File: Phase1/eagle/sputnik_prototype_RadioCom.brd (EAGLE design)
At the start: 99 x 100 mm, 104 parts, among them Y1 32MHz

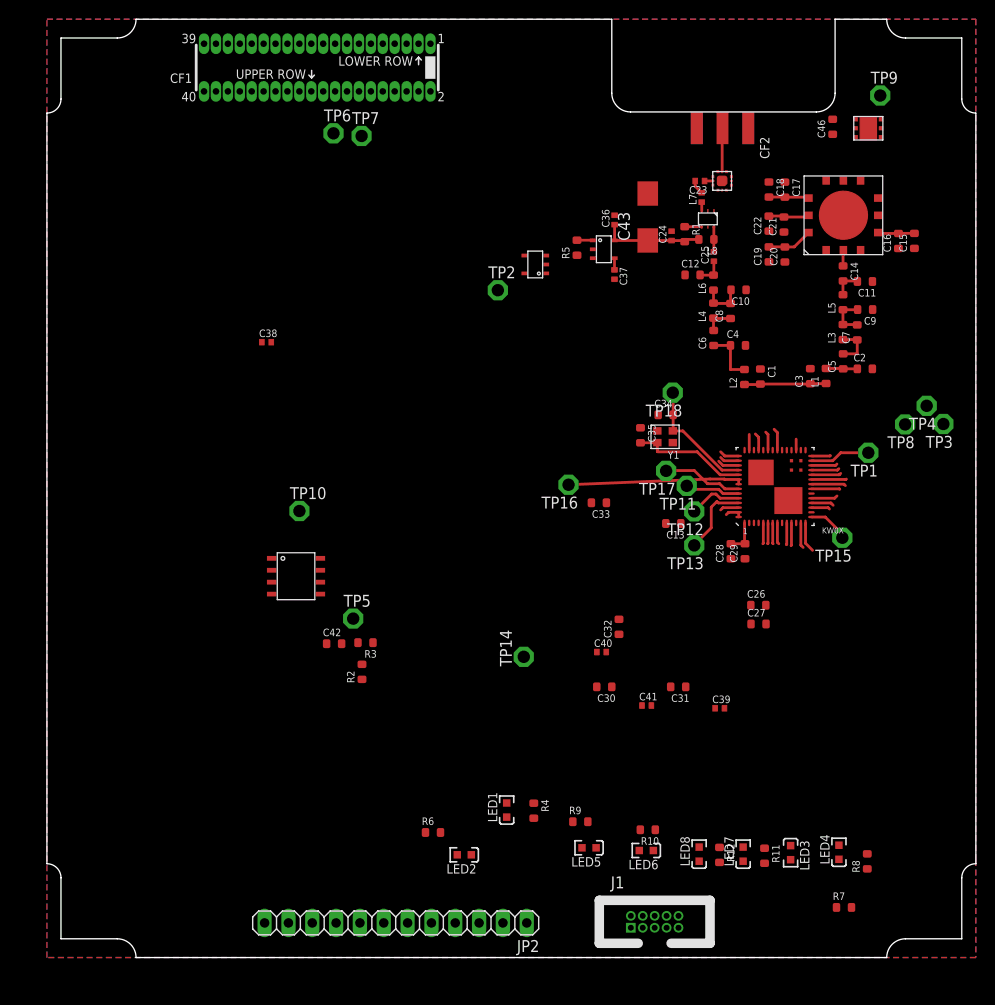
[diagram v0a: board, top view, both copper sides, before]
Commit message: Organized LED locations, test points, need to talk to Glenn about crossing RF paths because the switch inputs are reverse of the RFIO and PA_BOOST outputs.
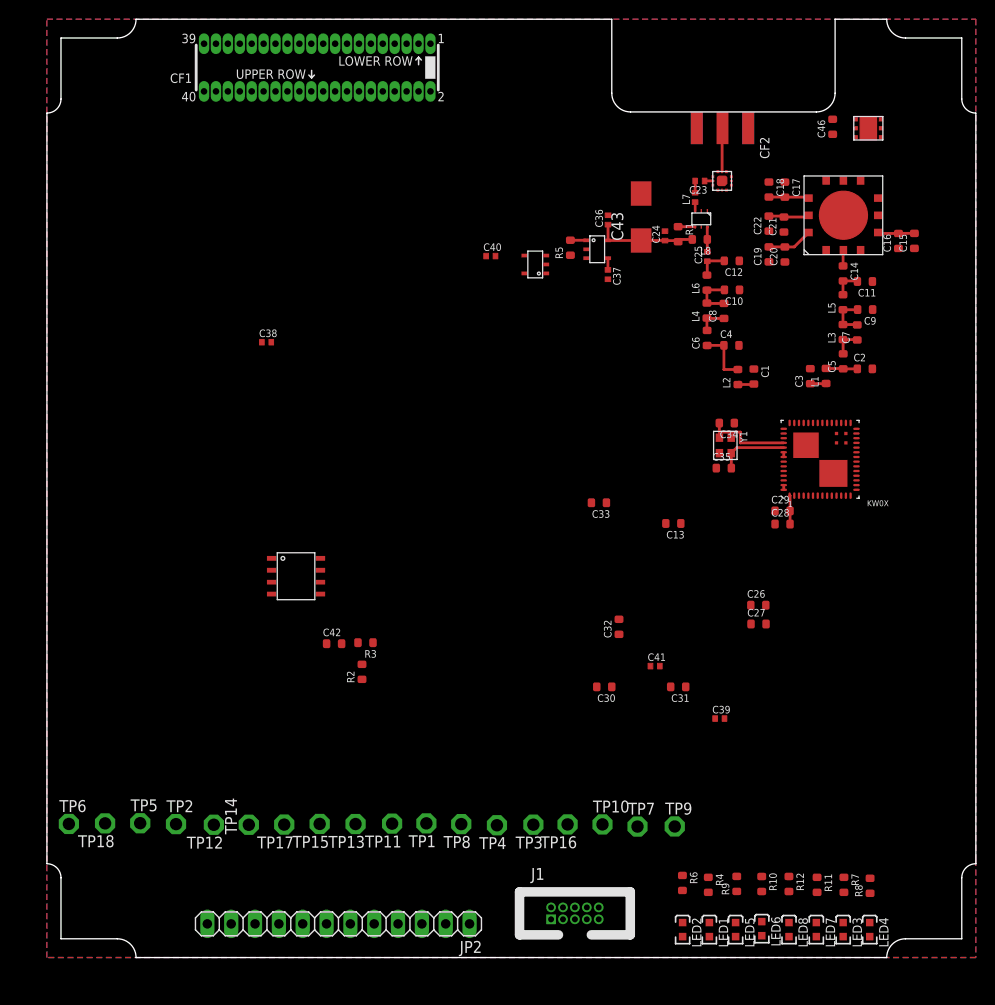
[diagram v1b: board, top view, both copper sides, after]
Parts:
- moved TP9 80.9 mm to (66.9, 14.0)
- moved TP7 79.3 mm to (62.9, 14.0)
- moved TP6 78.8 mm to (2.34, 14.2)
- moved TP18 75.9 mm to (6.20, 14.3)
- moved TP2 66.4 mm to (13.8, 14.2)
- moved TP4 64.0 mm to (48.0, 14.1)
- moved TP8 63.7 mm to (44.2, 14.2)
- moved TP15 63.5 mm to (29.1, 14.2)
- moved TP1 61.5 mm to (40.4, 14.3)
- moved TP12 61.1 mm to (17.8, 14.2)
- moved TP3 61.1 mm to (51.8, 14.2)
- moved TP17 55.5 mm to (25.3, 14.2)
- moved TP11 47.8 mm to (36.8, 14.3)
- moved TP13 46.7 mm to (32.9, 14.2)
- moved TP10 46.5 mm to (59.2, 14.2)
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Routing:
- net DIO0: track 18.7 -> 0.50 mm
- net 3.3V: track 13.0 -> 3.57 mm
- net DIO1: track 8.55 -> 0.00 mm
- net N$9: track 8.05 -> 0.00 mm
- net DIO5/CLKOUT: track 6.46 -> 0.00 mm
- net !CS: track 6.41 -> 0.00 mm
- net N$3: track 6.09 -> 0.00 mm
- net N$5: track 5.68 -> 0.00 mm
- net VR_PA: track 9.33 -> 4.01 mm
- net N$8: track 12.4 -> 7.45 mm
- net PTC4: track 3.74 -> 0.00 mm
- net PTB17: track 3.68 -> 0.00 mm
- net UART0_RX: track 3.23 -> 0.00 mm
- net PTC1: track 3.18 -> 0.00 mm
- net PTB2: track 3.04 -> 0.00 mm
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
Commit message: Attached SPI cache
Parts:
- moved C42 65.0 mm to (90.7, 58.4), turned to 270 degrees
- moved R2 64.7 mm to (91.9, 58.4)
- moved U$1 62.6 mm to (90.1, 54.9), turned to 0 degrees
- moved R3 60.8 mm to (93.2, 47.3), turned to 270 degrees
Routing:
- net MOSI: track 0.00 -> 19.4 mm
- net MISO: track 0.00 -> 18.5 mm, vias 0 -> 2
- net SCLK: track 0.00 -> 15.5 mm
- net !CS: track 0.00 -> 10.1 mm
- net !HOLD: track 0.00 -> 2.17 mm
- net N$11: track 0.00 -> 2.16 mm
- net 3.3V: track 3.57 -> 5.72 mm
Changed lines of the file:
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@@
 <attribute name="MFN-PN" value="AAT3215" x="57.86" y="74.06" size="1.778" layer="27" rot="R90" display="off"/>
 </element>
-<element name="U$1" library="psas_c3_team05" package="W25Q80DV" value="W25Q80DV" x="28.55" y="43.14" rot="R270"/>
-<element name="C42" library="rcl_custom" package=".0603-B-NOSILK" value="100nF" x="30.61" y="33.45"/>
+<element name="U$1" library="psas_c3_team05" package="W25Q80DV" value="W25Q80DV" x="90.06" y="54.85"/>
+<element name="C42" library="rcl_custom" package=".0603-B-NOSILK" value="100nF" x="90.65" y="58.39" rot="R270"/>
 <element name="TP9" library="testpad" package="P1-13" value="TPSPAD1-13" x="66.91" y="13.97">
 <attribute name="TP_SIGNAL_NAME" value="" x="66.91" y="13.97" size="1.778" layer="27" display="off"/>
@@
 <attribute name="TP_SIGNAL_NAME" value="" x="25.29" y="14.17" size="1.778" layer="27" rot="R180" display="off"/>
 </element>
-<element name="R2" library="rcl_custom" package=".0603-B-NOSILK" value="10k" x="33.58" y="30.45" rot="R90"/>
-<element name="R3" library="rcl_custom" package=".0603-B-NOSILK" value="10k" x="33.95" y="33.56" rot="R180"/>
+<element name="R2" library="rcl_custom" package=".0603-B-NOSILK" value="10k" x="91.9" y="58.4" rot="R90"/>
+<element name="R3" library="rcl_custom" package=".0603-B-NOSILK" value="10k" x="93.2" y="47.3" rot="R270"/>
 <element name="LED1" library="psas_c3_team05" package="LED-0603" value="" x="70.6" y="2.98" rot="R270">
 <attribute name="GREEN" value="" x="70.6" y="2.98" size="1.778" layer="27" rot="R270" display="off"/>
@@
 <wire x1="67.73" y1="8.75" x2="70.49" y2="8.55" width="0" layer="19" extent="1-1"/>
 <wire x1="17.1" y1="3.59" x2="67.73" y2="8.75" width="0" layer="19" extent="1-1"/>
-<wire x1="29.81" y1="33.45" x2="67.73" y2="8.75" width="0" layer="19" extent="1-1"/>
-<wire x1="23.95" y1="38.735" x2="29.81" y2="33.45" width="0" layer="19" extent="1-1"/>
-<wire x1="23.91" y1="65.58" x2="23.95" y2="38.735" width="0" layer="19" extent="1-1"/>
+<wire x1="90.65" y1="59.19" x2="67.73" y2="8.75" width="0" layer="19" extent="1-1"/>
+<wire x1="94.465" y1="50.25" x2="90.65" y2="59.19" width="0" layer="19" extent="1-1"/>
+<wire x1="23.91" y1="65.58" x2="94.465" y2="50.25" width="0" layer="19" extent="1-1"/>
 <wire x1="18.015" y1="92.31" x2="23.91" y2="65.58" width="0" layer="19" extent="1-1"/>
 <wire x1="16.745" y1="92.31" x2="18.015" y2="92.31" width="0" layer="19" extent="1-1"/>
@@
 <wire x1="53.73" y1="4.075" x2="87.69" y2="2.23" width="0" layer="19" extent="1-1"/>
 <wire x1="42.5" y1="3.59" x2="53.73" y2="4.075" width="0" layer="19" extent="1-1"/>
-<wire x1="33.58" y1="31.25" x2="58.6" y2="28.85" width="0" layer="19" extent="1-1"/>
-<wire x1="33.15" y1="33.56" x2="33.58" y2="31.25" width="0" layer="19" extent="1-1"/>
-<wire x1="31.41" y1="33.45" x2="33.15" y2="33.56" width="0" layer="19" extent="1-1"/>
-<wire x1="29.15" y1="42.545" x2="31.41" y2="33.45" width="0" layer="19" extent="1-1"/>
+<wire x1="91.9" y1="59.2" x2="58.6" y2="28.85" width="0" layer="19" extent="1-1"/>
+<wire x1="93.2" y1="46.5" x2="91.9" y2="59.2" width="0" layer="19" extent="1-1"/>
+<wire x1="90.65" y1="57.59" x2="93.2" y2="46.5" width="0" layer="19" extent="1-1"/>
 <wire x1="50.88" y1="72.915" x2="78.5222" y2="56.35" width="0" layer="19" extent="1-1"/>
 <wire x1="79.15" y1="49.2222" x2="79.2" y2="49.2222" width="0.3" layer="1"/>
 <wire x1="79.2" y1="49.2222" x2="79.2" y2="47.6" width="0.3" layer="1"/>
 <wire x1="79.2" y1="47.6" x2="79.2" y2="46.2" width="0.3" layer="1"/>
+<wire x1="90.655" y1="55.45" x2="90.65" y2="55.45" width="0.3" layer="1"/>
+<wire x1="90.65" y1="55.45" x2="90.65" y2="57.59" width="0.3" layer="1"/>
 </signal>
 <signal name="N$7">
@@
 <contactref element="TP10" pad="TP"/>
 <contactref element="R2" pad="1"/>
-<wire x1="33.58" y1="29.65" x2="29.15" y2="41.275" width="0" layer="19" extent="1-1"/>
-<wire x1="59.21" y1="14.19" x2="29.15" y2="41.275" width="0" layer="19" extent="1-1"/>
+<wire x1="59.21" y1="14.19" x2="91.925" y2="55.45" width="0" layer="19" extent="1-1"/>
+<wire x1="91.925" y1="55.45" x2="91.9" y2="55.45" width="0.3" layer="1"/>
+<wire x1="91.9" y1="55.45" x2="91.9" y2="57.6" width="0.3" layer="1"/>
 </signal>
 <signal name="!CS">
@@
 <contactref element="KW0X" pad="27"/>
 <contactref element="TP1" pad="TP"/>
-<wire x1="23.95" y1="42.545" x2="86.2778" y2="55.85" width="0" layer="19" extent="1-1"/>
-<wire x1="40.44" y1="14.3" x2="23.95" y2="42.545" width="0" layer="19" extent="1-1"/>
+<wire x1="40.44" y1="14.3" x2="90.655" y2="50.25" width="0" layer="19" extent="1-1"/>
+<wire x1="86.2778" y1="55.85" x2="89.7" y2="55.85" width="0.3" layer="1"/>
+<wire x1="89.7" y1="55.85" x2="89.7" y2="50.2" width="0.3" layer="1"/>
+<wire x1="89.7" y1="50.2" x2="90.655" y2="50.2" width="0.3" layer="1"/>
+<wire x1="90.655" y1="50.2" x2="90.655" y2="50.25" width="0.3" layer="1"/>
 </signal>
 <signal name="SCLK">
@@
 <contactref element="KW0X" pad="28"/>
 <contactref element="TP2" pad="TP"/>
-<wire x1="29.15" y1="40.005" x2="86.2778" y2="56.35" width="0" layer="19" extent="1-1"/>
-<wire x1="13.76" y1="14.22" x2="29.15" y2="40.005" width="0" layer="19" extent="1-1"/>
+<wire x1="13.76" y1="14.22" x2="93.195" y2="55.45" width="0" layer="19" extent="1-1"/>
+<wire x1="86.2778" y1="56.35" x2="89.7" y2="56.35" width="0.3" layer="1"/>
+<wire x1="89.7" y1="56.35" x2="89.7" y2="60.2" width="0.3" layer="1"/>
+<wire x1="89.7" y1="60.2" x2="93.195" y2="60.2" width="0.3" layer="1"/>
+<wire x1="93.195" y1="60.2" x2="93.195" y2="55.45" width="0.3" layer="1"/>
 </signal>
 <signal name="MISO">
@@
 <contactref element="KW0X" pad="29"/>
 <contactref element="TP3" pad="TP"/>
-<wire x1="23.95" y1="41.275" x2="85.65" y2="56.9778" width="0" layer="19" extent="1-1"/>
-<wire x1="51.84" y1="14.16" x2="23.95" y2="41.275" width="0" layer="19" extent="1-1"/>
+<wire x1="51.84" y1="14.16" x2="91.925" y2="50.25" width="0" layer="19" extent="1-1"/>
+<wire x1="85.65" y1="56.9778" x2="85.65" y2="57.8" width="0.3" layer="1"/>
+<wire x1="85.65" y1="57.8" x2="87.7" y2="57.8" width="0.3" layer="1"/>
+<via x="87.7" y="57.8" extent="1-16" drill="0.6" shape="octagon"/>
+<wire x1="87.7" y1="57.8" x2="87.7" y2="48.3" width="0.3" layer="16"/>
+<wire x1="87.7" y1="48.3" x2="91.9" y2="48.3" width="0.3" layer="16"/>
+<via x="91.9" y="48.3" extent="1-16" drill="0.6" shape="octagon"/>
+<wire x1="91.9" y1="48.3" x2="91.9" y2="50.25" width="0.3" layer="1"/>
+<wire x1="91.9" y1="50.25" x2="91.925" y2="50.25" width="0.3" layer="1"/>
 </signal>
 <signal name="MOSI">
@@
 <contactref element="KW0X" pad="31"/>
 <contactref element="TP4" pad="TP"/>
-<wire x1="29.15" y1="38.735" x2="84.65" y2="56.9778" width="0" layer="19" extent="1-1"/>
-<wire x1="47.96" y1="14.1" x2="29.15" y2="38.735" width="0" layer="19" extent="1-1"/>
+<wire x1="47.96" y1="14.1" x2="94.465" y2="55.45" width="0" layer="19" extent="1-1"/>
+<wire x1="84.65" y1="56.9778" x2="84.65" y2="58.6" width="0.3" layer="1"/>
+<wire x1="84.65" y1="58.6" x2="88.8" y2="58.6" width="0.3" layer="1"/>
+<wire x1="88.8" y1="58.6" x2="88.8" y2="61" width="0.3" layer="1"/>
+<wire x1="88.8" y1="61" x2="94.4" y2="61" width="0.3" layer="1"/>
+<wire x1="94.4" y1="61" x2="94.4" y2="55.45" width="0.3" layer="1"/>
+<wire x1="94.4" y1="55.45" x2="94.465" y2="55.45" width="0.3" layer="1"/>
 </signal>
 <signal name="PTC7">
@@
 <contactref element="R3" pad="1"/>
 <contactref element="TP5" pad="TP"/>
-<wire x1="23.95" y1="40.005" x2="34.75" y2="33.56" width="0" layer="19" extent="1-1"/>
-<wire x1="9.94" y1="14.32" x2="23.95" y2="40.005" width="0" layer="19" extent="1-1"/>
+<wire x1="9.94" y1="14.32" x2="93.195" y2="50.25" width="0" layer="19" extent="1-1"/>
+<wire x1="93.195" y1="50.25" x2="93.2" y2="50.25" width="0.3" layer="1"/>
+<wire x1="93.2" y1="50.25" x2="93.2" y2="48.1" width="0.3" layer="1"/>
 </signal>
 <signal name="N$12">

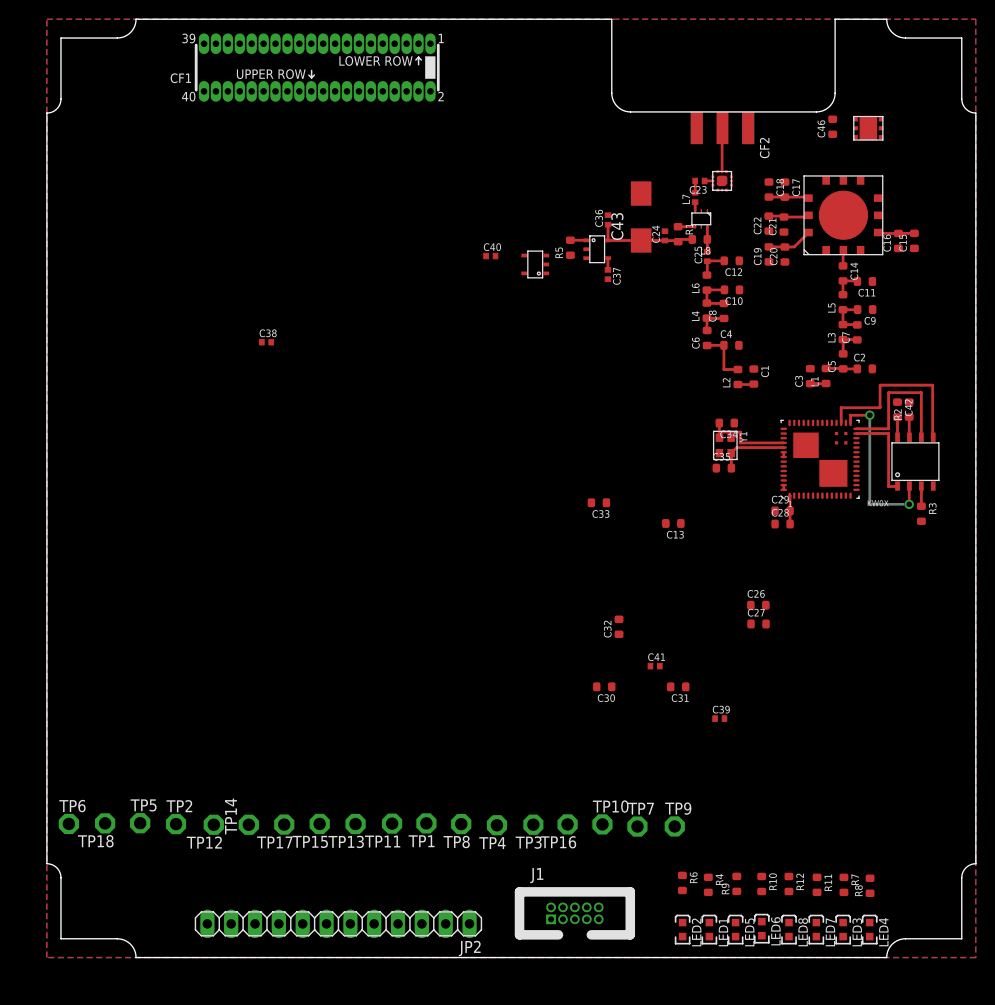
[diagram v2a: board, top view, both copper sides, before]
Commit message: Poor Jake. It's like there's some crazy guy screwing with him every time he commits... oh, wait. Huh. Anyway. Updated board outline with keepouts. Moved connectors into position and locked. Added shield over LNA (how could this be a bad idea? maybe the PA could use a sheild too, but with heat sinking?). Uncrossed the streams: make sure your main RF lines never, ever dive through the board. That sucks, keep it to one layer. So I had to move the PA and LNA around. Still needs some cleanup, but it's OK. Put resistors for sensitive supplies by the supplies, so no stray low impedance leakage.
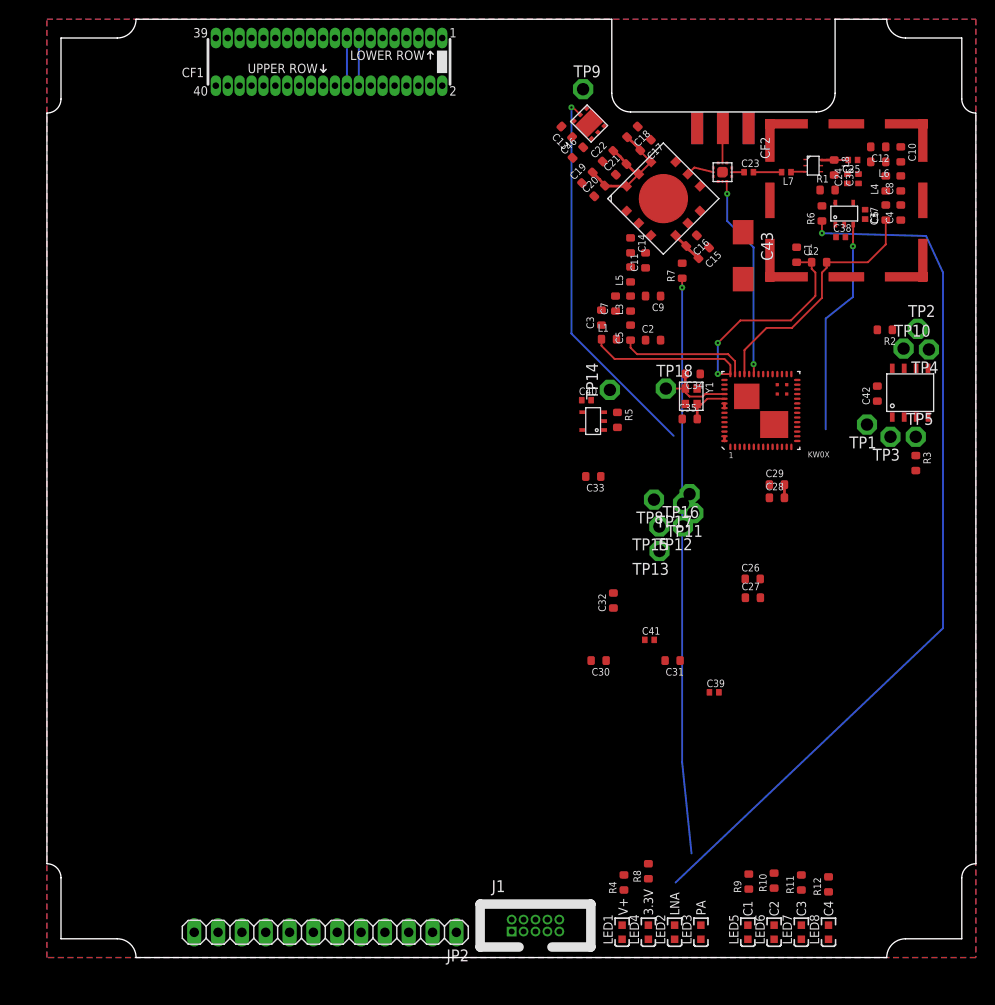
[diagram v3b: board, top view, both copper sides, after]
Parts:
- removed TP6, TP7: TPSPAD1-13, testpad:P1-13
- added SH1: BMI-S-202-SHIELD, hw-laird-bmi-s-202:BMI-S-202
- moved TP2 95.0 mm to (92.8, 67.0)
- moved TP5 92.3 mm to (92.6, 55.5)
- moved TP9 79.2 mm to (57.1, 92.5)
- moved TP18 75.6 mm to (66.0, 60.6), turned to 0 degrees
- moved R6 72.9 mm to (82.6, 79.3), turned to 90 degrees
- moved TP4 68.5 mm to (94.0, 64.8)
- moved R7 67.7 mm to (67.7, 73.2), turned to 90 degrees
- moved TP1 63.3 mm to (87.4, 56.8)
- moved C38 62.2 mm to (84.6, 76.8)
- moved TP14 60.2 mm to (60.0, 60.5)
- moved TP10 60.0 mm to (91.3, 64.9)
- moved TP12 59.3 mm to (67.8, 46.0)
- moved TP3 56.2 mm to (89.9, 55.5)
- moved TP17 54.6 mm to (67.8, 48.4)
- moved TP15 48.1 mm to (65.3, 45.9)
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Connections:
- removed net N$26: LED5.K, R9.2
- removed net N$29: LED6.K, R10.2
- removed net N$33: LED8.K, R12.2
- new net N$23: LED8.A, R12.1
- new net V_LNA_FILTERED: LED2.A, R6.1
- new net V_PA_FILTERED: LED3.A, R7.1
- net 3.3V: now also R8.2; no longer LED4.A
- net GND: now also LED1.K, LED2.K, LED3.K, LED4.K, LED5.K, LED6.K, LED7.K, LED8.K, SH1.P$1, SH1.P$10, SH1.P$11, SH1.P$12, SH1.P$2, SH1.P$3, SH1.P$4, SH1.P$5, SH1.P$6, SH1.P$7, SH1.P$8, SH1.P$9; no longer R10.1, R11.1, R12.1, R4.1, R6.1, R7.1, R8.1, R9.1
- net LNA_IN: now also TRSWITCH.2; no longer TRSWITCH.8
- net N$14: now also LED1.A, R4.1; no longer LED1.K, R4.2
- net N$15: now also LED5.A, R9.1; no longer LED2.K, R6.2
- net N$2: now also TRSWITCH.8; no longer TRSWITCH.2
- net N$20: now also LED6.A, R10.1; no longer LED3.K, R7.2
- net N$21: now also LED7.A, R11.1; no longer LED7.K, R11.2
- net N$22: now also LED4.A, R8.1; no longer LED4.K, R8.2
- net PTC1: now also R9.2; no longer LED5.A
- net PTC2: now also R10.2; no longer LED6.A
- net PTC3: now also R11.2; no longer LED7.A
- net PTC4: now also R12.2; no longer LED8.A
- net UART0_RX: no longer TP6.TP
- net UART0_TX: no longer TP7.TP
- net V+: now also R4.2; no longer LED1.A
- net VBIAS: now also R6.2; no longer LED2.A
- net VPA: now also R7.2; no longer LED3.A
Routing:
- net V_LNA_FILTERED: track 0.00 -> 93.9 mm, vias 0 -> 1
- net V_PA_FILTERED: track 0.00 -> 61.4 mm, vias 0 -> 1
- net PA_EN: track 0.00 -> 40.7 mm, vias 0 -> 1
- net VR_PA: track 4.01 -> 38.8 mm, vias 0 -> 2
- net LNA_EN: track 0.00 -> 23.2 mm, vias 0 -> 1
- net RXTX: track 0.00 -> 21.8 mm, vias 0 -> 2
- net RFIO: track 5.86 -> 26.8 mm
- net MOSI: track 19.4 -> 0.00 mm
- net MISO: track 18.5 -> 0.00 mm, vias 2 -> 0
- net SCLK: track 15.5 -> 0.00 mm
- net VBIAS: track 10.8 -> 0.09 mm
- net PA_BOOST: track 3.37 -> 13.9 mm
- net !CS: track 10.1 -> 0.00 mm
- net N$19: track 5.14 -> 0.00 mm
- net UART0_TX: track 0.00 -> 5.08 mm
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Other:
- board text added: "3.3V"
- board text added: "C1"
- board text added: "C2"
- board text added: "C3"
- board text added: "C4"
- board text added: "LNA"
- board text added: "PA"
- board text added: "V+"
- board text removed: "NEEDS POSITIONING"
